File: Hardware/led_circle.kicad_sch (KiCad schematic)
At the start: 59 parts

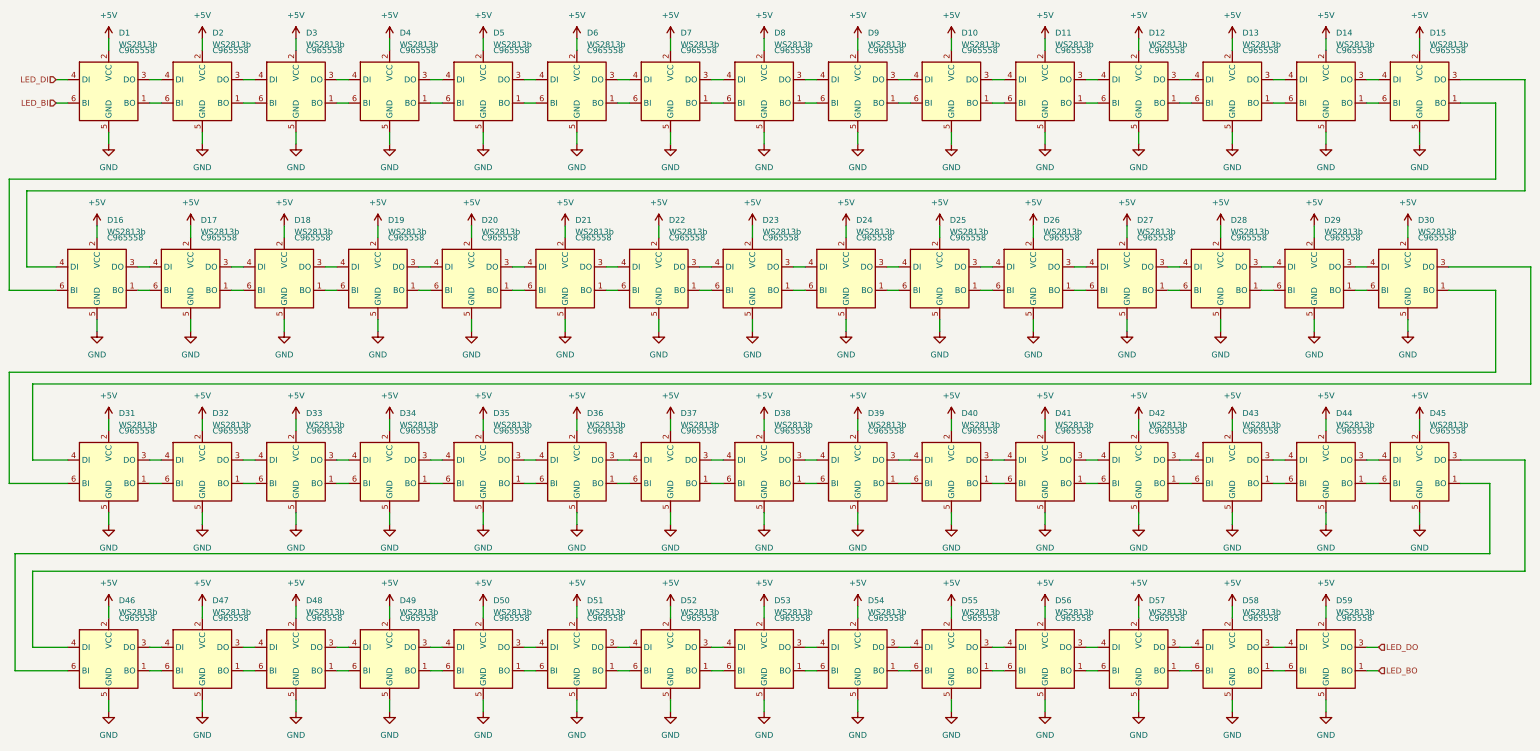
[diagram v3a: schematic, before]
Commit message: finalized layout, everything on top + LCSC numbers
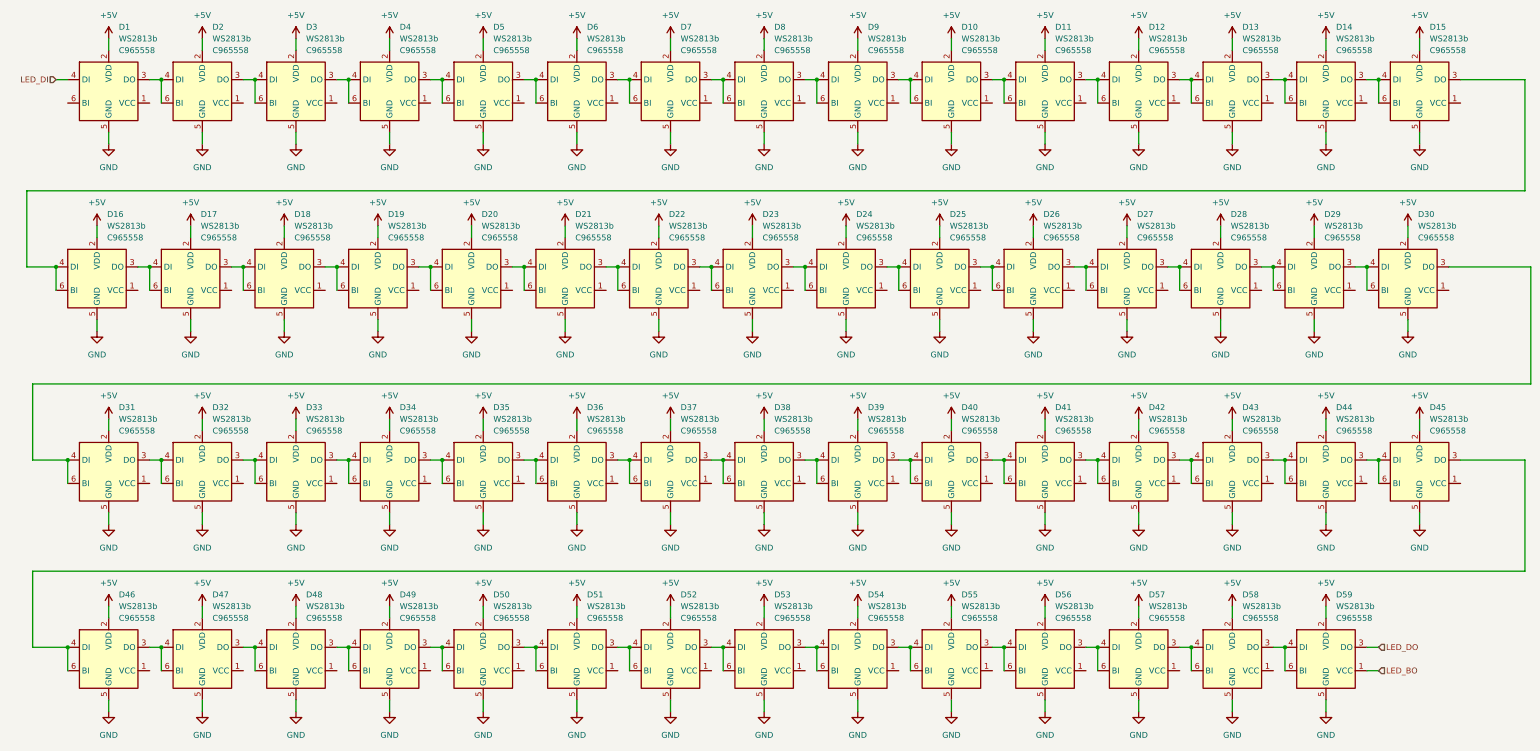
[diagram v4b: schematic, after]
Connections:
- net at D36.1 (VCC): no longer D37.6 (BI)
- net at D36.3 (DO), D37.4 (DI): now also D37.6 (BI)
- net at D35.3 (DO), D36.4 (DI): now also D36.6 (BI)
- net at D35.1 (VCC): no longer D36.6 (BI)
- net at D29.1 (VCC): no longer D30.6 (BI)
- net at D29.3 (DO), D30.4 (DI): now also D30.6 (BI)
- net at D28.3 (DO), D29.4 (DI): now also D29.6 (BI)
- net at D28.1 (VCC): no longer D29.6 (BI)
- net at D41.1 (VCC): no longer D42.6 (BI)
- net at D41.3 (DO), D42.4 (DI): now also D42.6 (BI)
- net at D40.3 (DO), D41.4 (DI): now also D41.6 (BI)
- net at D40.1 (VCC): no longer D41.6 (BI)
- net at D34.1 (VCC): no longer D35.6 (BI)
- net at D34.3 (DO), D35.4 (DI): now also D35.6 (BI)
- net at D33.3 (DO), D34.4 (DI): now also D34.6 (BI)
- net at D33.1 (VCC): no longer D34.6 (BI)
- net at D31.1 (VCC): no longer D32.6 (BI)
- net at D31.3 (DO), D32.4 (DI): now also D32.6 (BI)
- net at D30.3 (DO), D31.4 (DI): now also D31.6 (BI)
- net at D30.1 (VCC): no longer D31.6 (BI)
- net at D17.1 (VCC): no longer D18.6 (BI)
- net at D17.3 (DO), D18.4 (DI): now also D18.6 (BI)
- net at D16.3 (DO), D17.4 (DI): now also D17.6 (BI)
- net at D16.1 (VCC): no longer D17.6 (BI)
- net at D20.1 (VCC): no longer D21.6 (BI)
- net at D20.3 (DO), D21.4 (DI): now also D21.6 (BI)
- net at D19.3 (DO), D20.4 (DI): now also D20.6 (BI)
- net at D19.1 (VCC): no longer D20.6 (BI)
- net at D15.3 (DO), D16.4 (DI): now also D16.6 (BI)
- net at D15.1 (VCC): no longer D16.6 (BI)
- net at D47.1 (VCC): no longer D48.6 (BI)
- net at D47.3 (DO), D48.4 (DI): now also D48.6 (BI)
- net at D46.3 (DO), D47.4 (DI): now also D47.6 (BI)
- net at D46.1 (VCC): no longer D47.6 (BI)
- net at D7.1 (VCC): no longer D8.6 (BI)
- net at D7.3 (DO), D8.4 (DI): now also D8.6 (BI)
- net at D6.3 (DO), D7.4 (DI): now also D7.6 (BI)
- net at D6.1 (VCC): no longer D7.6 (BI)
- net at D4.1 (VCC): no longer D5.6 (BI)
- net at D4.3 (DO), D5.4 (DI): now also D5.6 (BI)
- net at D3.3 (DO), D4.4 (DI): now also D4.6 (BI)
- net at D3.1 (VCC): no longer D4.6 (BI)
- net at D48.1 (VCC): no longer D49.6 (BI)
- net at D48.3 (DO), D49.4 (DI): now also D49.6 (BI)
- net at D27.3 (DO), D28.4 (DI): now also D28.6 (BI)
- net at D27.1 (VCC): no longer D28.6 (BI)
- net at D18.1 (VCC): no longer D19.6 (BI)
- net at D18.3 (DO), D19.4 (DI): now also D19.6 (BI)
- net at D52.1 (VCC): no longer D53.6 (BI)
- net at D52.3 (DO), D53.4 (DI): now also D53.6 (BI)
- net at D51.3 (DO), D52.4 (DI): now also D52.6 (BI)
- net at D51.1 (VCC): no longer D52.6 (BI)
- net at D22.1 (VCC): no longer D23.6 (BI)
- net at D22.3 (DO), D23.4 (DI): now also D23.6 (BI)
- net at D21.3 (DO), D22.4 (DI): now also D22.6 (BI)
- net at D21.1 (VCC): no longer D22.6 (BI)
- net at D14.3 (DO), D15.4 (DI): now also D15.6 (BI)
- net at D14.1 (VCC): no longer D15.6 (BI)
- net at D45.3 (DO), D46.4 (DI): now also D46.6 (BI)
- net at D45.1 (VCC): no longer D46.6 (BI)
- net at D53.1 (VCC): no longer D54.6 (BI)
- net at D53.3 (DO), D54.4 (DI): now also D54.6 (BI)
- net at D26.3 (DO), D27.4 (DI): now also D27.6 (BI)
- net at D26.1 (VCC): no longer D27.6 (BI)
- net at D38.1 (VCC): no longer D39.6 (BI)
- net at D38.3 (DO), D39.4 (DI): now also D39.6 (BI)
- net at D37.3 (DO), D38.4 (DI): now also D38.6 (BI)
- net at D37.1 (VCC): no longer D38.6 (BI)
- net at D8.1 (VCC): no longer D9.6 (BI)
- net at D8.3 (DO), D9.4 (DI): now also D9.6 (BI)
- net at D5.1 (VCC): no longer D6.6 (BI)
- net at D5.3 (DO), D6.4 (DI): now also D6.6 (BI)
- net at D32.3 (DO), D33.4 (DI): now also D33.6 (BI)
- net at D32.1 (VCC): no longer D33.6 (BI)
- net at D39.1 (VCC): no longer D40.6 (BI)
- net at D39.3 (DO), D40.4 (DI): now also D40.6 (BI)
- net at D25.3 (DO), D26.4 (DI): now also D26.6 (BI)
- net at D25.1 (VCC): no longer D26.6 (BI)
- net at D9.1 (VCC): no longer D10.6 (BI)
- net at D10.4 (DI), D9.3 (DO): now also D10.6 (BI)
- net at D56.1 (VCC): no longer D57.6 (BI)
- net at D56.3 (DO), D57.4 (DI): now also D57.6 (BI)
- net at D55.3 (DO), D56.4 (DI): now also D56.6 (BI)
- net at D55.1 (VCC): no longer D56.6 (BI)
- net at D50.1 (VCC): no longer D51.6 (BI)
- net at D50.3 (DO), D51.4 (DI): now also D51.6 (BI)
- net at D49.3 (DO), D50.4 (DI): now also D50.6 (BI)
- net at D49.1 (VCC): no longer D50.6 (BI)
- net at D10.1 (VCC): no longer D11.6 (BI)
- net at D10.3 (DO), D11.4 (DI): now also D11.6 (BI)
- net at D1.1 (VCC): no longer D2.6 (BI)
- net at D1.3 (DO), D2.4 (DI): now also D2.6 (BI)
- net at D12.1 (VCC): no longer D13.6 (BI)
- net at D12.3 (DO), D13.4 (DI): now also D13.6 (BI)
- net at D11.3 (DO), D12.4 (DI): now also D12.6 (BI)
- net at D11.1 (VCC): no longer D12.6 (BI)
- net at D42.1 (VCC): no longer D43.6 (BI)
- net at D42.3 (DO), D43.4 (DI): now also D43.6 (BI)
- net at D2.3 (DO), D3.4 (DI): now also D3.6 (BI)
- net at D2.1 (VCC): no longer D3.6 (BI)
- net at D44.1 (VCC): no longer D45.6 (BI)
- net at D44.3 (DO), D45.4 (DI): now also D45.6 (BI)
- net at D43.3 (DO), D44.4 (DI): now also D44.6 (BI)
- net at D43.1 (VCC): no longer D44.6 (BI)
- net at D54.1 (VCC): no longer D55.6 (BI)
- net at D54.3 (DO), D55.4 (DI): now also D55.6 (BI)
- net at D23.1 (VCC): no longer D24.6 (BI)
- net at D23.3 (DO), D24.4 (DI): now also D24.6 (BI)
- net at D13.1 (VCC): no longer D14.6 (BI)
- net at D13.3 (DO), D14.4 (DI): now also D14.6 (BI)
- net at D58.1 (VCC): no longer D59.6 (BI)
- net at D58.3 (DO), D59.4 (DI): now also D59.6 (BI)
- net at D57.3 (DO), D58.4 (DI): now also D58.6 (BI)
- net at D57.1 (VCC): no longer D58.6 (BI)
- net at D24.3 (DO), D25.4 (DI): now also D25.6 (BI)
- net at D24.1 (VCC): no longer D25.6 (BI)
- net LED_BI: no longer names the net of D1.6 (BI)

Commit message: finalized layout, via stitching
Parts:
- D1, D10, D11, D12, D13, D14, D15, D16, D17, D18, D19, D2, D20, D21, D22, D23, D24, D25, D26, D27, D28, D29, D3, D30, D31, D32, D33, D34, D35, D36, D37, D38, D39, D4, D40, D41, D42, D43, D44, D45, D46, D47, D48, D49, D5, D50, D51, D52, D53, D54, D55, D56, D57, D58, D59, D6, D7, D8, D9: LCSC C965558 -> C114592
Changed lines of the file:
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@@
 			)
 		)
-		(property "LCSC" "C965558"
+		(property "LCSC" "C114592"
 			(at 160.9441 129.54 0)
 			(effects
@@
 			)
 		)
-		(property "LCSC" "C965558"
+		(property "LCSC" "C114592"
 			(at 320.9641 87.63 0)
 			(effects
@@
 			)
 		)
-		(property "LCSC" "C965558"
+		(property "LCSC" "C114592"
 			(at 262.5441 129.54 0)
 			(effects
@@
 			)
 		)
-		(property "LCSC" "C965558"
+		(property "LCSC" "C114592"
 			(at 120.3041 129.54 0)
 			(effects
@@
 			)
 		)
-		(property "LCSC" "C965558"
+		(property "LCSC" "C114592"
 			(at 59.3441 129.54 0)
 			(effects
@@
 			)
 		)
-		(property "LCSC" "C965558"
+		(property "LCSC" "C114592"
 			(at 77.1241 87.63 0)
 			(effects
@@
 			)
 		)
-		(property "LCSC" "C965558"
+		(property "LCSC" "C114592"
 			(at 138.0841 87.63 0)
 			(effects
@@
 			)
 		)
-		(property "LCSC" "C965558"
+		(property "LCSC" "C114592"
 			(at 56.8041 87.63 0)
 			(effects
@@
 			)
 		)
-		(property "LCSC" "C965558"
+		(property "LCSC" "C114592"
 			(at 79.6641 170.18 0)
 			(effects
@@
 			)
 		)
-		(property "LCSC" "C965558"
+		(property "LCSC" "C114592"
 			(at 341.2841 87.63 0)
 			(effects
@@
 			)
 		)
-		(property "LCSC" "C965558"
+		(property "LCSC" "C114592"
 			(at 181.2641 46.99 0)
 			(effects
@@
 			)
 		)
-		(property "LCSC" "C965558"
+		(property "LCSC" "C114592"
 			(at 140.6241 129.54 0)
 			(effects
@@
 			)
 		)
-		(property "LCSC" "C965558"
+		(property "LCSC" "C114592"
 			(at 120.3041 46.99 0)
 			(effects
@@
 			)
 		)
-		(property "LCSC" "C965558"
+		(property "LCSC" "C114592"
 			(at 99.9841 170.18 0)
 			(effects
@@
 			)
 		)
-		(property "LCSC" "C965558"
+		(property "LCSC" "C114592"
 			(at 300.6441 87.63 0)
 			(effects
@@
 			)
 		)
-		(property "LCSC" "C965558"
+		(property "LCSC" "C114592"
 			(at 97.4441 87.63 0)
 			(effects
@@
 			)
 		)
-		(property "LCSC" "C965558"
+		(property "LCSC" "C114592"
 			(at 181.2641 170.18 0)
 			(effects
@@
 			)
 		)
-		(property "LCSC" "C965558"
+		(property "LCSC" "C114592"
 			(at 178.7241 87.63 0)
 			(effects
@@
 			)
 		)
-		(property "LCSC" "C965558"
+		(property "LCSC" "C114592"
 			(at 343.8241 46.99 0)
 			(effects
@@
 			)
 		)
-		(property "LCSC" "C965558"
+		(property "LCSC" "C114592"
 			(at 59.3441 170.18 0)
 			(effects
@@
 			)
 		)
-		(property "LCSC" "C965558"
+		(property "LCSC" "C114592"
 			(at 201.5841 170.18 0)
 			(effects
@@
 			)
 		)
-		(property "LCSC" "C965558"
+		(property "LCSC" "C114592"
 			(at 117.7641 87.63 0)
 			(effects
@@
 			)
 		)
-		(property "LCSC" "C965558"
+		(property "LCSC" "C114592"
 			(at 280.3241 87.63 0)
 			(effects
@@
 			)
 		)
-		(property "LCSC" "C965558"
+		(property "LCSC" "C114592"
 			(at 158.4041 87.63 0)
 			(effects
@@
 			)
 		)
-		(property "LCSC" "C965558"
+		(property "LCSC" "C114592"
 			(at 201.5841 129.54 0)
 			(effects
@@
 			)
 		)
-		(property "LCSC" "C965558"
+		(property "LCSC" "C114592"
 			(at 201.5841 46.99 0)
 			(effects
@@
 			)
 		)
-		(property "LCSC" "C965558"
+		(property "LCSC" "C114592"
 			(at 140.6241 46.99 0)
 			(effects
@@
 			)
 		)
-		(property "LCSC" "C965558"
+		(property "LCSC" "C114592"
 			(at 99.9841 129.54 0)
 			(effects
@@
 			)
 		)
-		(property "LCSC" "C965558"
+		(property "LCSC" "C114592"
 			(at 181.2641 129.54 0)
 			(effects
@@
 			)
 		)
-		(property "LCSC" "C965558"
+		(property "LCSC" "C114592"
 			(at 221.9041 129.54 0)
 			(effects
@@
 			)
 		)
-		(property "LCSC" "C965558"
+		(property "LCSC" "C114592"
 			(at 260.0041 87.63 0)
 			(effects
@@
 			)
 		)
-		(property "LCSC" "C965558"
+		(property "LCSC" "C114592"
 			(at 242.2241 129.54 0)
 			(effects
@@
 			)
 		)
-		(property "LCSC" "C965558"
+		(property "LCSC" "C114592"
 			(at 221.9041 46.99 0)
 			(effects
@@
 			)
 		)
-		(property "LCSC" "C965558"
+		(property "LCSC" "C114592"
 			(at 160.9441 46.99 0)
 			(effects
@@
 			)
 		)
-		(property "LCSC" "C965558"
+		(property "LCSC" "C114592"
 			(at 262.5441 170.18 0)
 			(effects
@@
 			)
 		)
-		(property "LCSC" "C965558"
+		(property "LCSC" "C114592"
 			(at 79.6641 129.54 0)
 			(effects
@@
 			)
 		)
-		(property "LCSC" "C965558"
+		(property "LCSC" "C114592"
 			(at 140.6241 170.18 0)
 			(effects
@@
 			)
 		)
-		(property "LCSC" "C965558"
+		(property "LCSC" "C114592"
 			(at 242.2241 46.99 0)
 			(effects
@@
 			)
 		)
-		(property "LCSC" "C965558"
+		(property "LCSC" "C114592"
 			(at 59.3441 46.99 0)
 			(effects
@@
 			)
 		)
-		(property "LCSC" "C965558"
+		(property "LCSC" "C114592"
 			(at 282.8641 46.99 0)
 			(effects
@@
 			)
 		)
-		(property "LCSC" "C965558"
+		(property "LCSC" "C114592"
 			(at 282.8641 129.54 0)
 			(effects
@@
 			)
 		)
-		(property "LCSC" "C965558"
+		(property "LCSC" "C114592"
 			(at 99.9841 46.99 0)
 			(effects
@@
 			)
 		)
-		(property "LCSC" "C965558"
+		(property "LCSC" "C114592"
 			(at 323.5041 129.54 0)
 			(effects
@@
 			)
 		)
-		(property "LCSC" "C965558"
+		(property "LCSC" "C114592"
 			(at 221.9041 170.18 0)
 			(effects
@@
 			)
 		)
-		(property "LCSC" "C965558"
+		(property "LCSC" "C114592"
 			(at 199.0441 87.63 0)
 			(effects
@@
 			)
 		)
-		(property "LCSC" "C965558"
+		(property "LCSC" "C114592"
 			(at 303.1841 129.54 0)
 			(effects
@@
 			)
 		)
-		(property "LCSC" "C965558"
+		(property "LCSC" "C114592"
 			(at 303.1841 46.99 0)
 			(effects
@@
 			)
 		)
-		(property "LCSC" "C965558"
+		(property "LCSC" "C114592"
 			(at 303.1841 170.18 0)
 			(effects
@@
 			)
 		)
-		(property "LCSC" "C965558"
+		(property "LCSC" "C114592"
 			(at 343.8241 129.54 0)
 			(effects
@@
 			)
 		)
-		(property "LCSC" "C965558"
+		(property "LCSC" "C114592"
 			(at 323.5041 46.99 0)
 			(effects
@@
 			)
 		)
-		(property "LCSC" "C965558"
+		(property "LCSC" "C114592"
 			(at 262.5441 46.99 0)
 			(effects
@@
 			)
 		)
-		(property "LCSC" "C965558"
+		(property "LCSC" "C114592"
 			(at 242.2241 170.18 0)
 			(effects
@@
 			)
 		)
-		(property "LCSC" "C965558"
+		(property "LCSC" "C114592"
 			(at 120.3041 170.18 0)
 			(effects
@@
 			)
 		)
-		(property "LCSC" "C965558"
+		(property "LCSC" "C114592"
 			(at 323.5041 170.18 0)
 			(effects
@@
 			)
 		)
-		(property "LCSC" "C965558"
+		(property "LCSC" "C114592"
 			(at 282.8641 170.18 0)
 			(effects
@@
 			)
 		)
-		(property "LCSC" "C965558"
+		(property "LCSC" "C114592"
 			(at 79.6641 46.99 0)
 			(effects
@@
 			)
 		)
-		(property "LCSC" "C965558"
+		(property "LCSC" "C114592"
 			(at 239.6841 87.63 0)
 			(effects
@@
 			)
 		)
-		(property "LCSC" "C965558"
+		(property "LCSC" "C114592"
 			(at 219.3641 87.63 0)
 			(effects
@@
 			)
 		)
-		(property "LCSC" "C965558"
+		(property "LCSC" "C114592"
 			(at 160.9441 170.18 0)
 			(effects

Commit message: updated lcsc numbers
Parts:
- D1, D10, D11, D12, D13, D14, D15, D16, D17, D18, D19, D2, D20, D21, D22, D23, D24, D25, D26, D27, D28, D29, D3, D30, D31, D32, D33, D34, D35, D36, D37, D38, D39, D4, D40, D41, D42, D43, D44, D45, D46, D47, D48, D49, D5, D50, D51, D52, D53, D54, D55, D56, D57, D58, D59, D6, D7, D8, D9: lcsc_new (none) -> C114592
